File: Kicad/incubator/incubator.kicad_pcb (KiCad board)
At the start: 2 copper layers, 99.1 x 73.7 mm, 41 parts, among them J1 Barrel_Jack_MountingPin, J2 Conn_01x06, J3 Conn_01x01, J4 RJ12, J5 Conn_01x01, J6 Conn_01x01, J7 Conn_01x01, SW2 Rotary_Encoder_Switch, U1 AP63205WU, U2 ATmega328P-AU

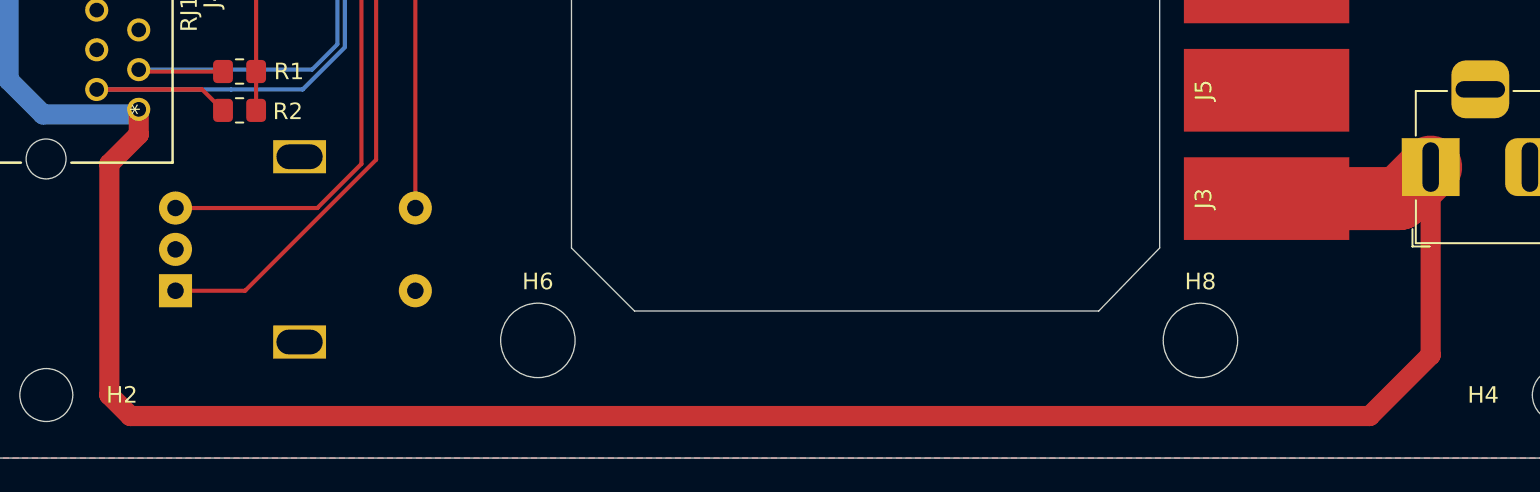
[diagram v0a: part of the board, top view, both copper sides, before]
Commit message: fix: fan size and push button position and news routes
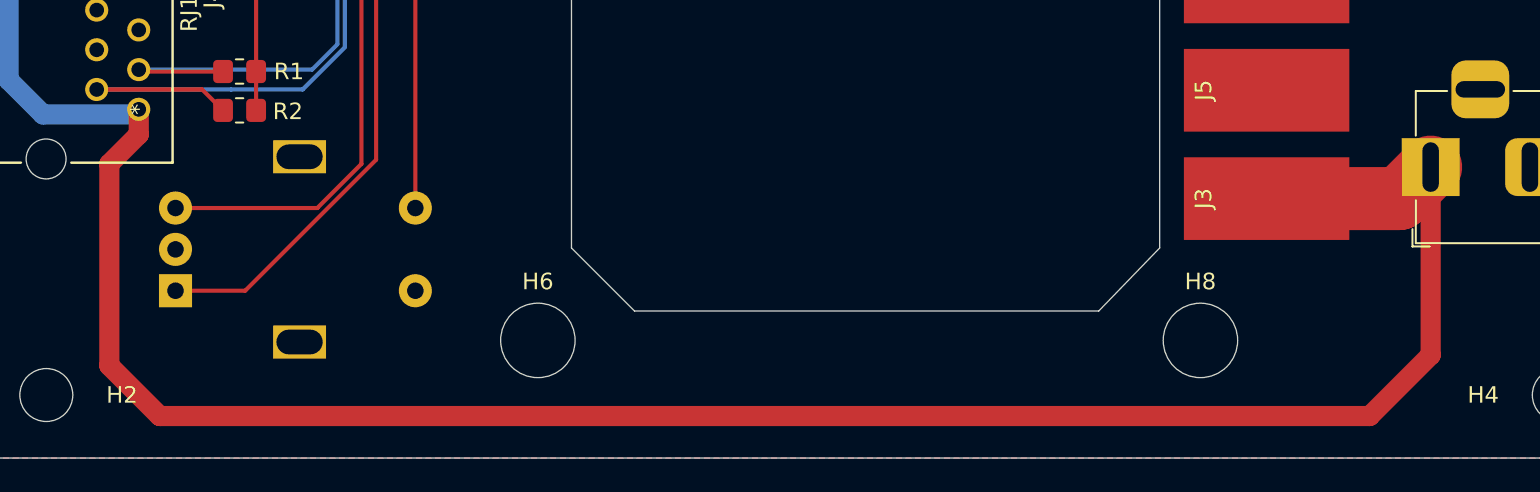
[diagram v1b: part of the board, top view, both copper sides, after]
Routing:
- net 12V: track 193.2 -> 192.2 mm
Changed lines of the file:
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@@
   (general
     (thickness 1.6)
-    (drawings 17)
+    (drawings 19)
     (tracks 281)
     (zones 0)
@@
   )
   (setup
-    (last_trace_width 0.25)
+    (last_trace_width 1.2192)
     (user_trace_width 0.6096)
     (user_trace_width 1.2192)
@@
     )
   )
+  (dimension 40.005072 (width 0.15) (layer Dwgs.User)
+    (gr_text "40.005 mm" (at 112.01093 -27.04157 89.89115176) (layer Dwgs.User)
+      (effects (font (size 1 1) (thickness 0.15)))
+    )
+    (feature1 (pts (xy 73.66 -47.117) (xy 111.335352 -47.045426)))
+    (feature2 (pts (xy 73.584 -7.112) (xy 111.259352 -7.040426)))
+    (crossbar (pts (xy 110.672932 -7.04154) (xy 110.748932 -47.04654)))
+    (arrow1a (pts (xy 110.748932 -47.04654) (xy 111.333212 -45.918924)))
+    (arrow1b (pts (xy 110.748932 -47.04654) (xy 110.160372 -45.921152)))
+    (arrow2a (pts (xy 110.672932 -7.04154) (xy 111.261492 -8.166928)))
+    (arrow2b (pts (xy 110.672932 -7.04154) (xy 110.088652 -8.169156)))
+  )
+  (dimension 37.338 (width 0.15) (layer Dwgs.User)
+    (gr_text "37.338 mm" (at 107.853 -25.781 90) (layer Dwgs.User)
+      (effects (font (size 1 1) (thickness 0.15)))
+    )
+    (feature1 (pts (xy 73.584 -44.45) (xy 107.139421 -44.45)))
+    (feature2 (pts (xy 73.584 -7.112) (xy 107.139421 -7.112)))
+    (crossbar (pts (xy 106.553 -7.112) (xy 106.553 -44.45)))
+    (arrow1a (pts (xy 106.553 -44.45) (xy 107.139421 -43.323496)))
+    (arrow1b (pts (xy 106.553 -44.45) (xy 105.966579 -43.323496)))
+    (arrow2a (pts (xy 106.553 -7.112) (xy 107.139421 -8.238504)))
+    (arrow2b (pts (xy 106.553 -7.112) (xy 105.966579 -8.238504)))
+  )
   (gr_line (start 35.56 -38.1) (end 35.56 -12.7) (layer Edge.Cuts) (width 0.05))
   (gr_line (start 39.37 -41.91) (end 35.56 -38.1) (layer Edge.Cuts) (width 0.05))
@@
   (segment (start 21.1455 -65.4685) (end 19.939 -64.262) (width 0.25) (layer F.Cu) (net 2))
   (segment (start 85.598 -15.6845) (end 87.503 -17.5895) (width 3.81) (layer F.Cu) (net 2))
-  (segment (start 9.398 -21.082) (end 9.398 -19.558) (width 1.2192) (layer F.Cu) (net 2))
-  (segment (start 9.398 -19.558) (end 7.62 -17.78) (width 1.2192) (layer F.Cu) (net 2))
-  (segment (start 7.62 -17.78) (end 7.62 -3.81) (width 1.2192) (layer F.Cu) (net 2))
-  (segment (start 7.62 -3.81) (end 8.89 -2.54) (width 1.2192) (layer F.Cu) (net 2))
-  (segment (start 8.89 -2.54) (end 83.82 -2.54) (width 1.2192) (layer F.Cu) (net 2))
-  (segment (start 87.503 -6.223) (end 87.503 -17.5895) (width 1.2192) (layer F.Cu) (net 2))
-  (segment (start 83.82 -2.54) (end 87.503 -6.223) (width 1.2192) (layer F.Cu) (net 2))
   (segment (start 18.709 -62.524) (end 18.709 -64.011) (width 0.6096) (layer F.Cu) (net 2))
   (via (at 18.709 -62.524) (size 0.8) (drill 0.4) (layers F.Cu B.Cu) (net 2))
@@
   (segment (start 9.398 -21.082) (end 9.089899 -20.773899) (width 1.2192) (layer B.Cu) (net 2))
   (segment (start 77.584 -15.6845) (end 85.598 -15.6845) (width 3.81) (layer F.Cu) (net 2))
+  (segment (start 9.398 -19.558) (end 9.398 -21.082) (width 1.2192) (layer F.Cu) (net 2))
+  (segment (start 7.62 -17.78) (end 9.398 -19.558) (width 1.2192) (layer F.Cu) (net 2))
+  (segment (start 7.62 -5.588) (end 7.62 -17.78) (width 1.2192) (layer F.Cu) (net 2))
+  (segment (start 83.82 -2.54) (end 10.668 -2.54) (width 1.2192) (layer F.Cu) (net 2))
+  (segment (start 10.668 -2.54) (end 7.62 -5.588) (width 1.2192) (layer F.Cu) (net 2))
+  (segment (start 87.503 -6.223) (end 83.82 -2.54) (width 1.2192) (layer F.Cu) (net 2))
+  (segment (start 87.503 -17.5895) (end 87.503 -6.223) (width 1.2192) (layer F.Cu) (net 2))
   (segment (start 18.034 -55.88) (end 18.034 -57.15) (width 0.25) (layer F.Cu) (net 3))
   (segment (start 18.034 -57.15) (end 17.3355 -57.8485) (width 0.25) (layer F.Cu) (net 3))
